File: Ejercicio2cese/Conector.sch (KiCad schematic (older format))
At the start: 6 parts, among them J2 CAN, U2 AMIS42665TJAA1RG

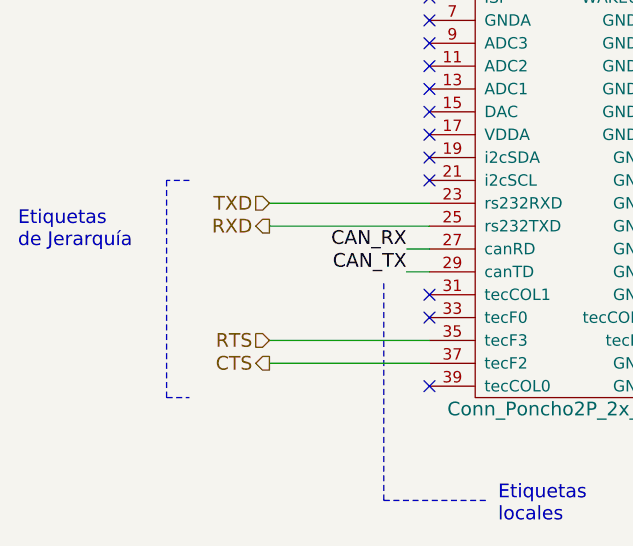
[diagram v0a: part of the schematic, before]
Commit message: Agrego RS232 multipart al esquemático. Cambio nombres de líneas seriales.
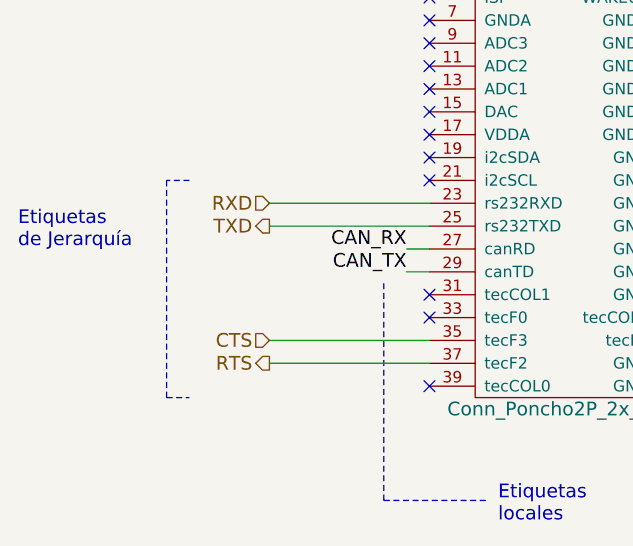
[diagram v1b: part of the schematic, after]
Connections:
- net CTS: now also XA1.35 (tecF3); no longer XA1.37 (tecF2)
- net RTS: now also XA1.37 (tecF2); no longer XA1.35 (tecF3)
- net RXD: now also XA1.23 (rs232RXD); no longer XA1.25 (rs232TXD)
- net TXD: now also XA1.25 (rs232TXD); no longer XA1.23 (rs232RXD)
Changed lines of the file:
@@
 LIBS:power
 LIBS:fiducial
+LIBS:max232_mp
 LIBS:ej2-cache
 EELAYER 25 0
@@
 Wire Wire Line
 	5050 3750 4350 3750
+Text HLabel 4350 3850 0    60   Output ~ 0
+TXD
 Text HLabel 4350 3750 0    60   Input ~ 0
-TXD
-Text HLabel 4350 3850 0    60   Output ~ 0
 RXD
 Wire Wire Line
@@
 Wire Wire Line
 	5050 4450 4350 4450
+Text HLabel 4350 4450 0    60   Output ~ 0
+RTS
 Text HLabel 4350 4350 0    60   Input ~ 0
-RTS
-Text HLabel 4350 4450 0    60   Output ~ 0
 CTS
 NoConn ~ 6250 4350
